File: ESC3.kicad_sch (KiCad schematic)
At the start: 34 parts, among them J11 SWD3, J12 MOTOR3, Q10 XRS306D, Q8 XRS306D, Q9 XRS306D, U11 STM32G071GBUxN, U12 DRV8300D

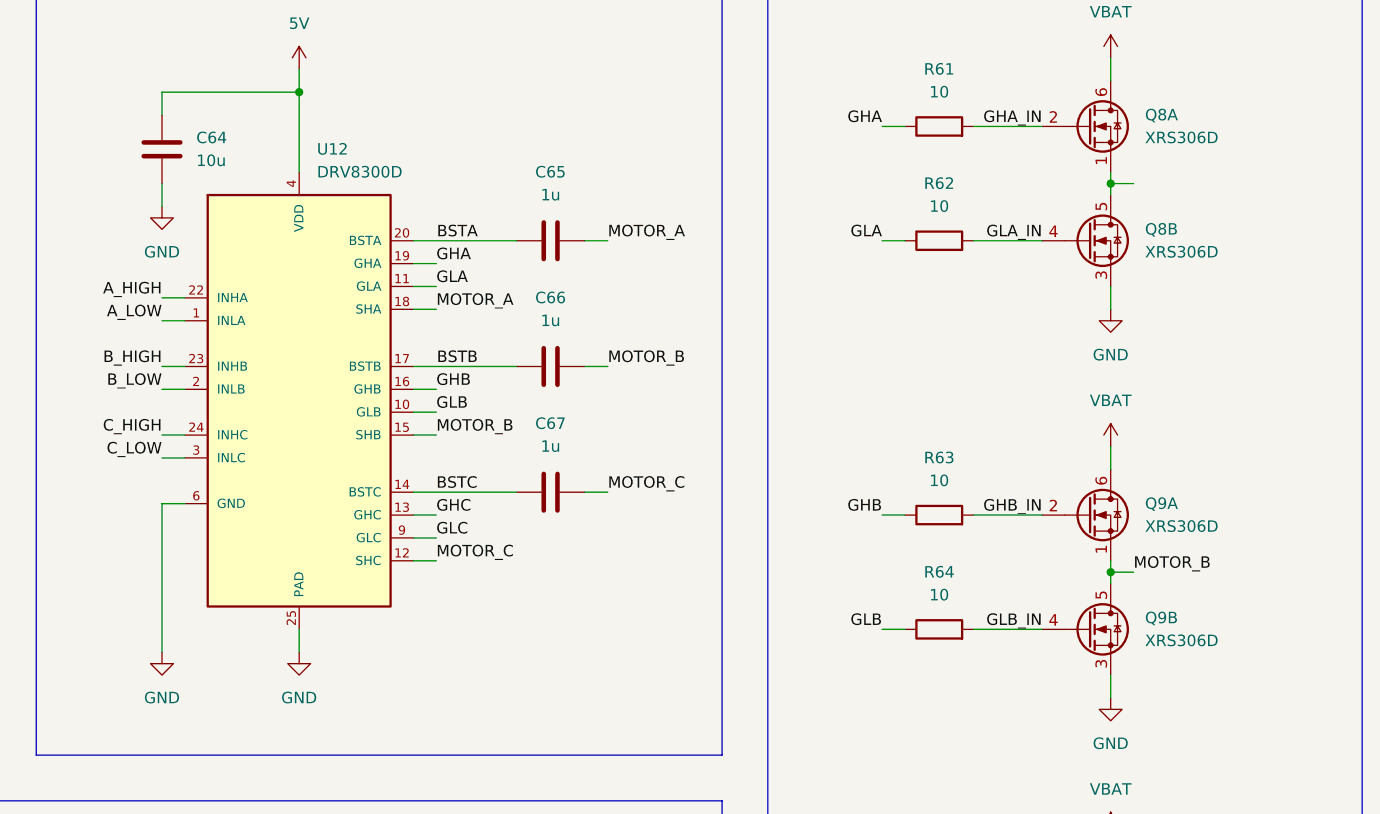
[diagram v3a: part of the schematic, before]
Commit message: Missing labels and revision
First complete revision of the schematic.
Added missing labels.

TODO:
Continue reviewing the schematic.
Include net coloring.
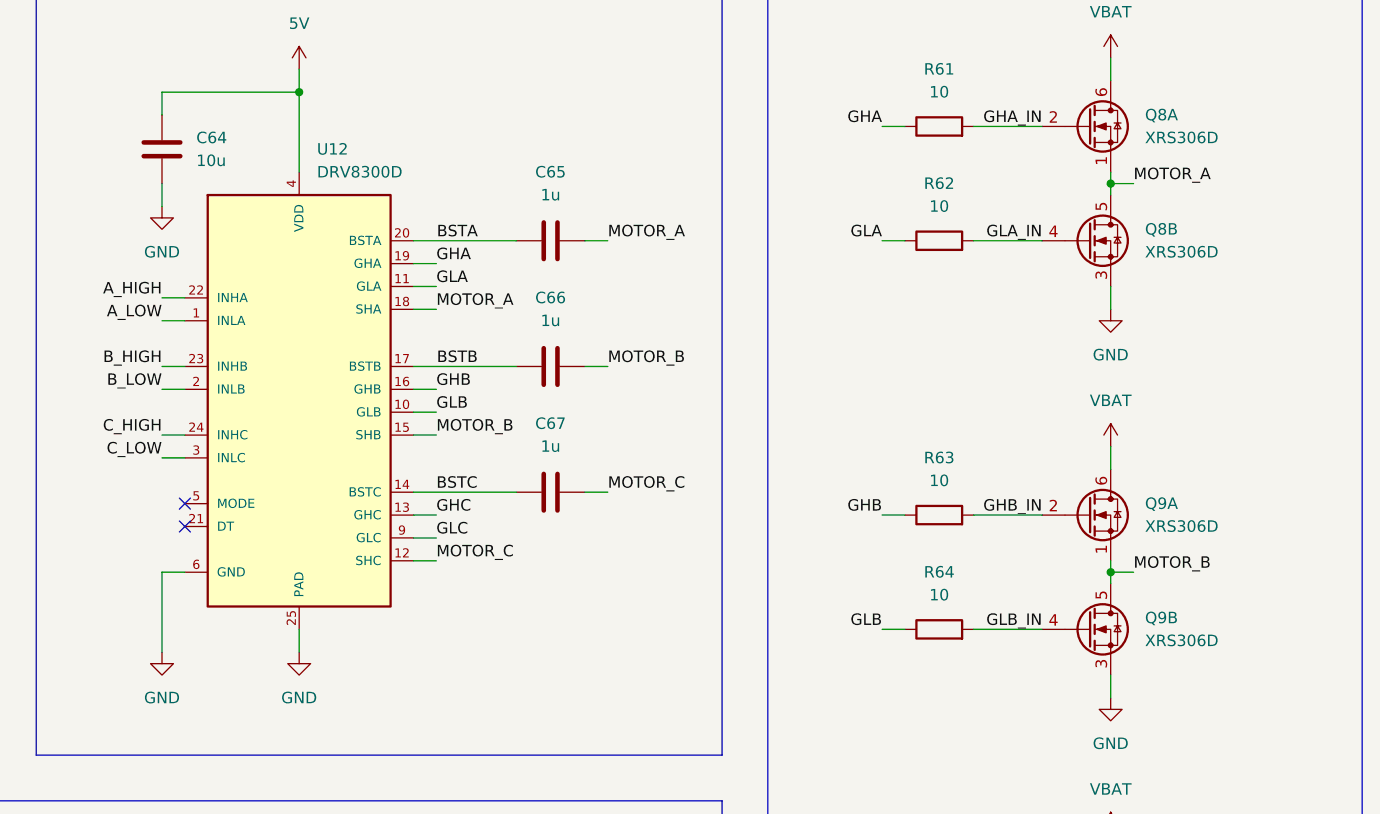
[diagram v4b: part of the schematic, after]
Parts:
- C58, C60, C61, C62, C63: footprint (none) -> Capacitor_SMD:C_1206_3216Metric
- J11: footprint (none) -> Custom_Parts:PAD_2_SQUARE_SOLID_1.0x1.0mm_P1.5mm
- Q10, Q8, Q9: footprint Custom_Parts:PDFN8 -> Custom_Parts:PDFN8_DUAL_3.3x3.3mm
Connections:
- net MOTOR_A: now also Q8.1 (S), Q8.5 (D)
- no-connect marks 13 -> 15
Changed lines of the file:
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@@
 	)
 	(no_connect
+		(at 143.51 81.28)
+	)
+	(no_connect
 		(at 50.8 80.01)
 	)
@@
 	)
 	(no_connect
+		(at 143.51 83.82)
+	)
+	(no_connect
 		(at 50.8 49.53)
 	)
@@
 	(wire
 		(pts
+			(xy 143.51 88.9) (xy 140.97 88.9)
+		)
+		(stroke
+			(width 0)
+			(type default)
+		)
+	)
+	(wire
+		(pts
 			(xy 151.13 133.35) (xy 153.67 133.35)
 		)
@@
 	(wire
 		(pts
-			(xy 143.51 81.28) (xy 140.97 81.28)
+			(xy 140.97 88.9) (xy 140.97 97.79)
 		)
 		(stroke
@@
 	(wire
 		(pts
-			(xy 140.97 81.28) (xy 140.97 97.79)
-		)
-		(stroke
-			(width 0)
-			(type default)
-		)
-	)
-	(wire
-		(pts
 			(xy 62.23 171.45) (xy 62.23 172.72)
 		)
@@
 		)
 	)
+	(label "MOTOR_A"
+		(at 248.92 45.72 0)
+		(effects
+			(font
+				(size 1.27 1.27)
+			)
+			(justify left bottom)
+		)
+	)
 	(label "GHB"
 		(at 220.98 82.55 180)
@@
 			)
 		)
-		(property "Footprint" "Custom_Parts:PDFN8"
+		(property "Footprint" "Custom_Parts:PDFN8_DUAL_3.3x3.3mm"
 			(at 248.92 39.37 0)
 			(effects
@@
 			)
 		)
-		(property "Footprint" ""
+		(property "Footprint" "Capacitor_SMD:C_1206_3216Metric"
 			(at 37.7952 180.34 0)
 			(effects
@@
 			)
 		)
-		(property "Footprint" "Custom_Parts:PDFN8"
+		(property "Footprint" "Custom_Parts:PDFN8_DUAL_3.3x3.3mm"
 			(at 248.92 52.07 0)
 			(effects
@@
 	)
 	(symbol
-		(lib_id "power:GND")
-		(at 140.97 97.79 0)
-		(unit 1)
-		(exclude_from_sim no)
-		(in_bom yes)
-		(on_board yes)
-		(dnp no)
-		(fields_autoplaced yes)
-		(property "Reference" "#PWR0116"
-			(at 140.97 104.14 0)
-			(effects
-				(font
-					(size 1.27 1.27)
-				)
-				(hide yes)
-			)
-		)
-		(property "Value" "GND"
-			(at 140.97 102.87 0)
-			(effects
-				(font
-					(size 1.27 1.27)
-				)
-			)
-		)
-		(property "Footprint" ""
-			(at 140.97 97.79 0)
-			(effects
-				(font
-					(size 1.27 1.27)
-				)
-				(hide yes)
-			)
-		)
-		(property "Datasheet" ""
-			(at 140.97 97.79 0)
-			(effects
-				(font
-					(size 1.27 1.27)
-				)
-				(hide yes)
-			)
-		)
-		(property "Description" "Power symbol creates a global label with name \"GND\" , ground"
-			(at 140.97 97.79 0)
-			(effects
-				(font
-					(size 1.27 1.27)
-				)
-				(hide yes)
-			)
-		)
-		(pin "1"
-		)
-		(instances
-			(project "ThunderHorse"
-				(path "/ac187c6c-fa53-41cc-bce1-6f39a42a92e8/807a5f6f-4255-4cf0-8d90-acd62bb18590/f6401a6f-b04c-410e-81b5-25d3c51023df"
-					(reference "#PWR0116")
-					(unit 1)
-				)
-			)
-		)
-	)
-	(symbol
 		(lib_id "Device:R")
 		(at 144.78 133.35 90)
@@
 			)
 		)
-		(property "Footprint" "Custom_Parts:PDFN8"
+		(property "Footprint" "Custom_Parts:PDFN8_DUAL_3.3x3.3mm"
 			(at 248.92 125.73 0)
 			(effects
@@
 			)
 		)
-		(property "Footprint" "Custom_Parts:PDFN8"
+		(property "Footprint" "Custom_Parts:PDFN8_DUAL_3.3x3.3mm"
 			(at 248.92 82.55 0)
 			(effects
@@
 			)
 		)
-		(property "Footprint" "Custom_Parts:PDFN8"
+		(property "Footprint" "Custom_Parts:PDFN8_DUAL_3.3x3.3mm"
 			(at 248.92 138.43 0)
 			(effects
@@
 		(pin "4"
 		)
+		(pin "7"
+		)
+		(pin "8"
+		)
+		(pin "21"
+		)
+		(pin "5"
+		)
 		(instances
 			(project "ThunderHorse"
@@
 			)
 		)
-		(property "Footprint" ""
+		(property "Footprint" "Capacitor_SMD:C_1206_3216Metric"
 			(at 50.4952 180.34 0)
 			(effects
@@
 			)
 		)
-		(property "Footprint" "Custom_Parts:PDFN8"
+		(property "Footprint" "Custom_Parts:PDFN8_DUAL_3.3x3.3mm"
 			(at 248.92 95.25 0)
 			(effects
@@
 			)
 		)
-		(property "Footprint" ""
+		(property "Footprint" "Capacitor_SMD:C_1206_3216Metric"
 			(at 88.5952 180.34 0)
 			(effects
@@
 			)
 		)
-		(property "Footprint" ""
+		(property "Footprint" "Capacitor_SMD:C_1206_3216Metric"
 			(at 63.1952 180.34 0)
 			(effects
@@
 			)
 		)
-		(property "Footprint" ""
+		(property "Footprint" "Custom_Parts:PAD_2_SQUARE_SOLID_1.0x1.0mm_P1.5mm"
 			(at 102.87 77.47 0)
 			(effects
@@
 			)
 		)
-		(property "Footprint" ""
+		(property "Footprint" "Capacitor_SMD:C_1206_3216Metric"
 			(at 75.8952 180.34 0)
 			(effects
@@
 					(unit 1)
 				)
+			)
+		)
+	)
+	(symbol
+		(lib_id "power:GND")
+		(at 140.97 97.79 0)
+		(unit 1)
+		(exclude_from_sim no)
+		(in_bom yes)
+		(on_board yes)
+		(dnp no)
+		(fields_autoplaced yes)
+		(property "Reference" "#PWR0116"
+			(at 140.97 104.14 0)
+			(effects
+				(font
+					(size 1.27 1.27)
+				)
+				(hide yes)
+			)
+		)
+		(property "Value" "GND"
+			(at 140.97 102.87 0)
+			(effects
+				(font
+					(size 1.27 1.27)
+				)
+			)
+		)
+		(property "Footprint" ""
+			(at 140.97 97.79 0)
+			(effects
+				(font
+					(size 1.27 1.27)
+				)
+				(hide yes)
+			)
+		)
+		(property "Datasheet" ""
+			(at 140.97 97.79 0)
+			(effects
+				(font
+					(size 1.27 1.27)
+				)
+				(hide yes)
+			)
+		)
+		(property "Description" "Power symbol creates a global label with name \"GND\" , ground"
+			(at 140.97 97.79 0)
+			(effects
+				(font
+					(size 1.27 1.27)
+				)
+				(hide yes)
+			)
+		)
+		(pin "1"
+		)
+		(instances
+			(project "ThunderHorse"
+				(path "/ac187c6c-fa53-41cc-bce1-6f39a42a92e8/807a5f6f-4255-4cf0-8d90-acd62bb18590/f6401a6f-b04c-410e-81b5-25d3c51023df"
+					(reference "#PWR0116")
+					(unit 1)
+				)

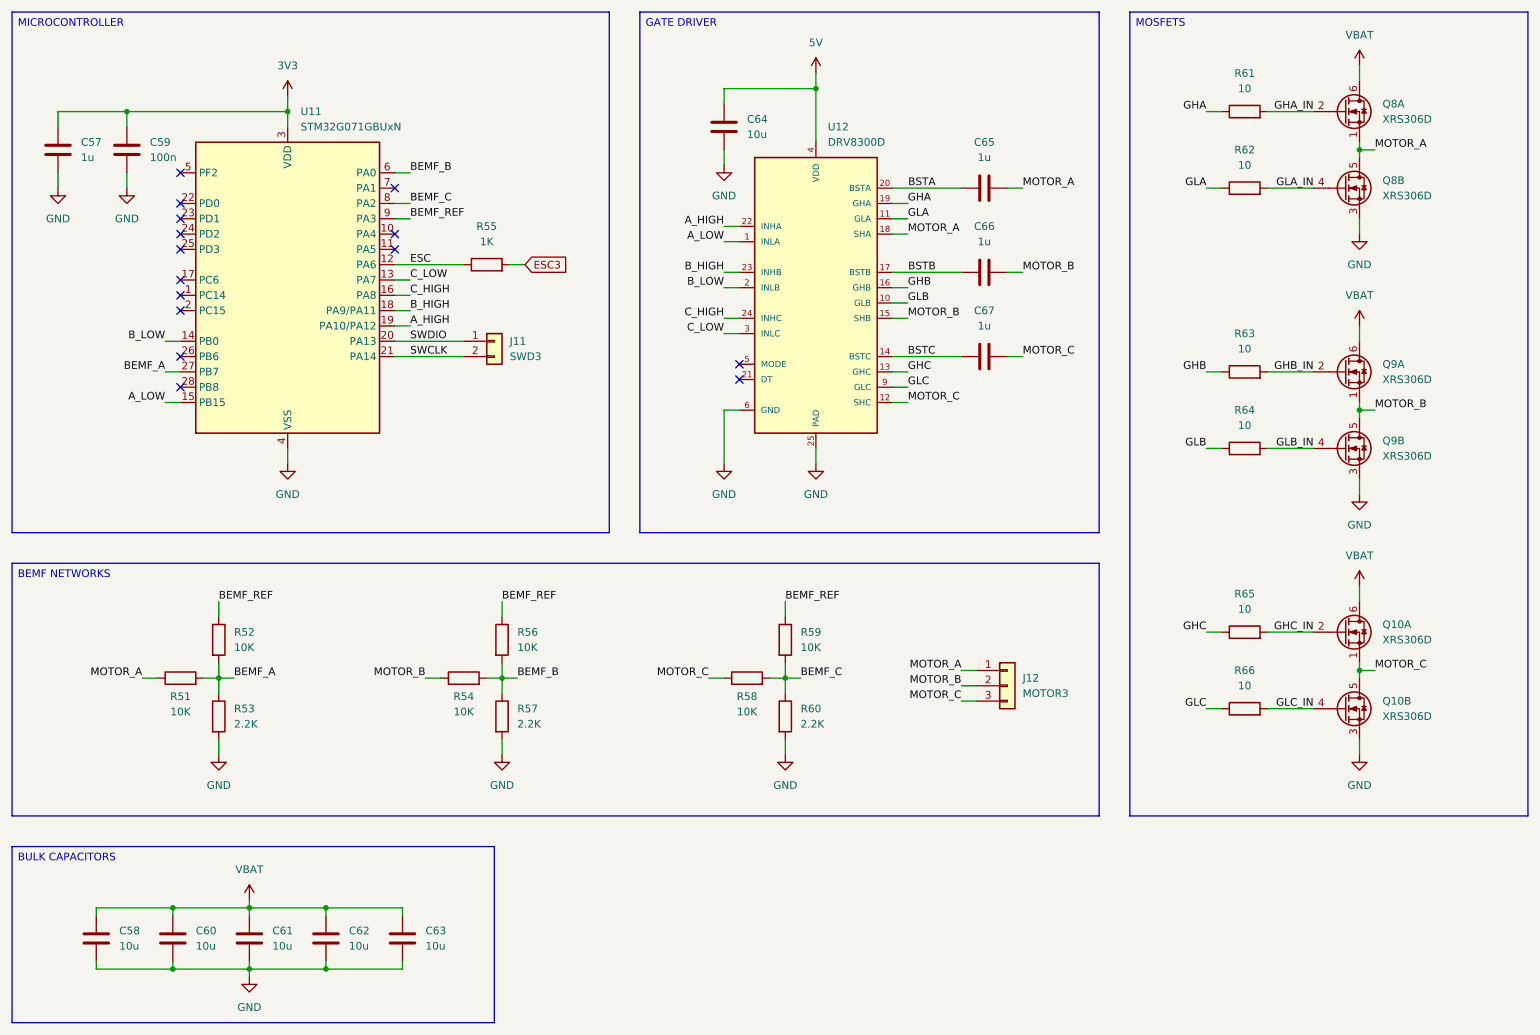
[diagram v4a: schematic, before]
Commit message: ESC layout and footprints
Added the initial ESC layout.
Updated some footprints for compatibility.
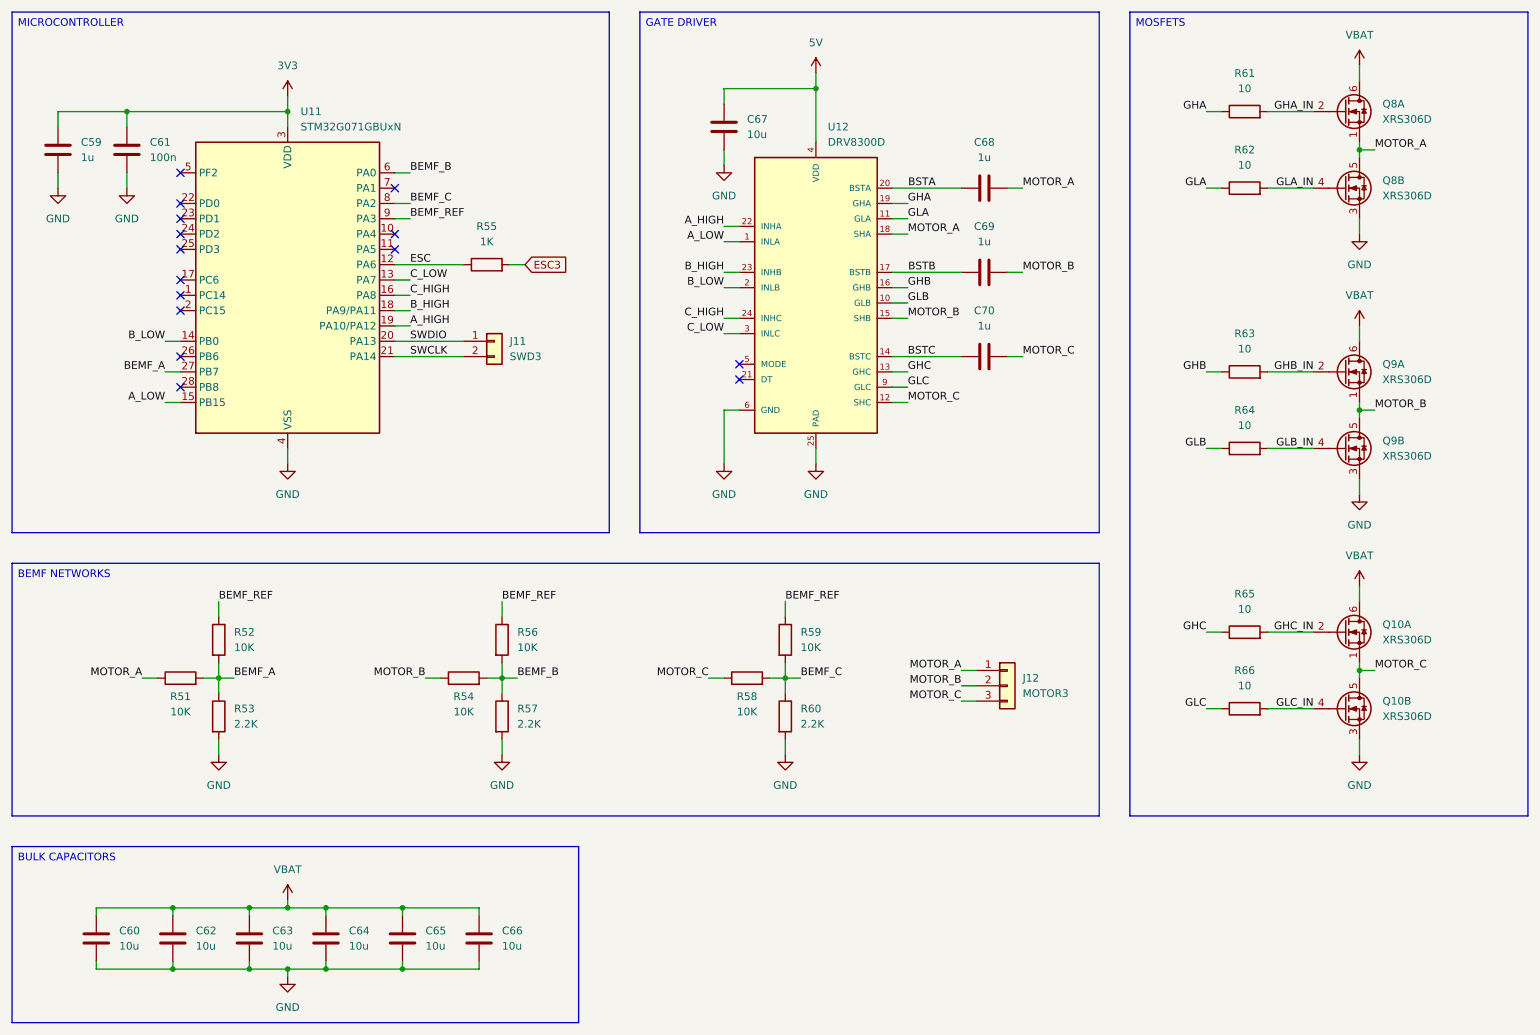
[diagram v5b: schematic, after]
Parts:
- removed C58, C61: 10u, Capacitor_SMD:C_1206_3216Metric, symbol Device:C
- added C64, C65, C66: 10u, Capacitor_SMD:C_1206_3216Metric, symbol Device:C
- J12: footprint Custom_Parts:PAD_3_SQUARE_SOLID_2.0x2.0mm_P2.5mm -> Custom_Parts:PAD_3_SQUARE_SOLID_2.5x2.5mm_P4.0mm
- renumbered C57 to C59, C59 to C61, C64 to C67, C65 to C68, C66 to C69, C67 to C70
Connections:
- net GND: now also C64.2, C65.2, C66.2
- net VBAT: now also C64.1, C65.1, C66.1

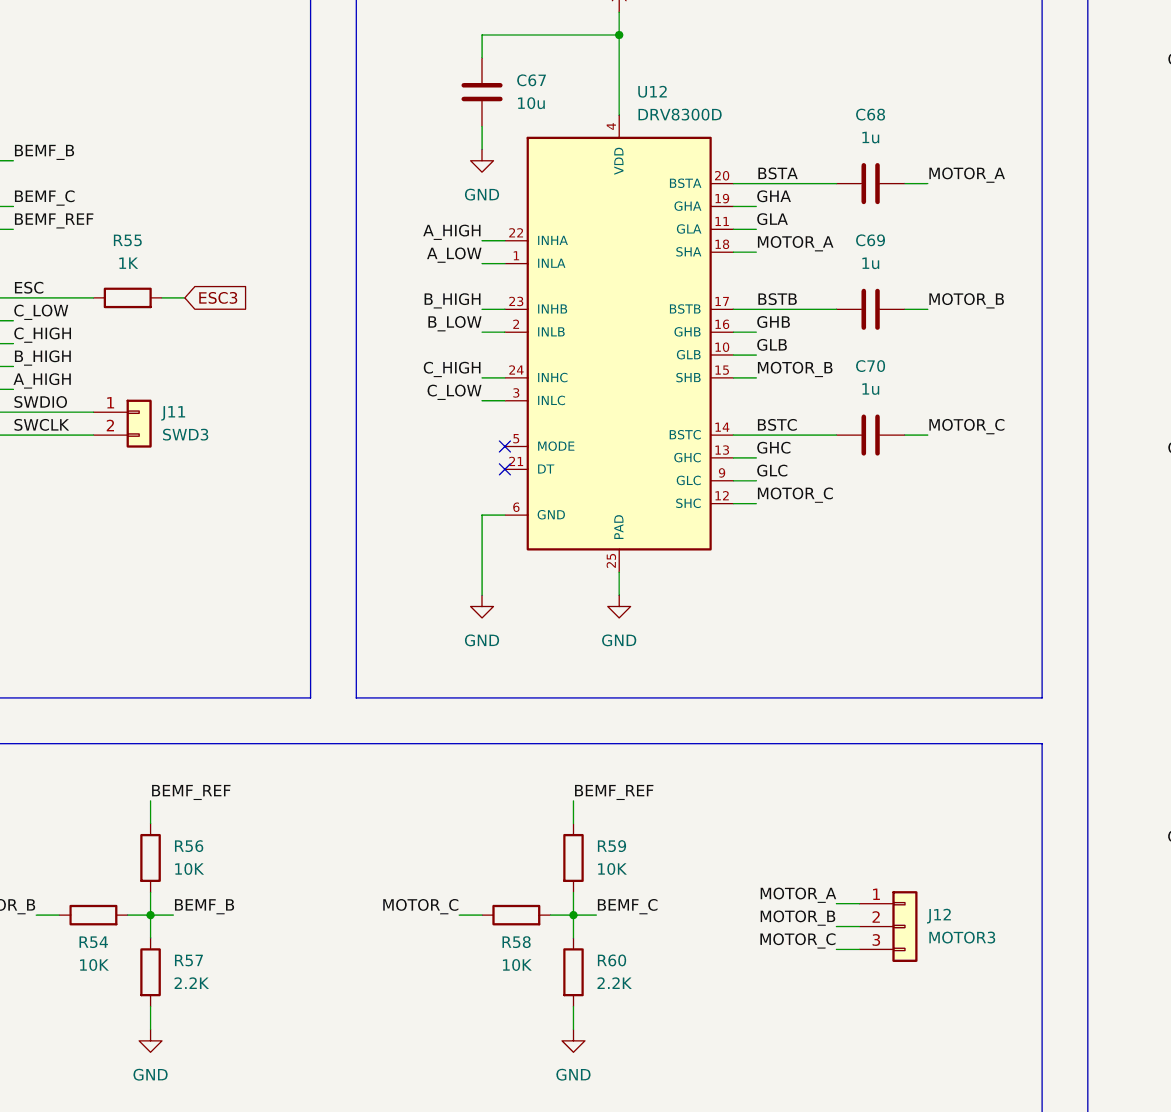
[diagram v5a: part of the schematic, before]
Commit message: Layout replication
Updated the ESC schematic to allow for layout replication.
Updated the PCB layout.
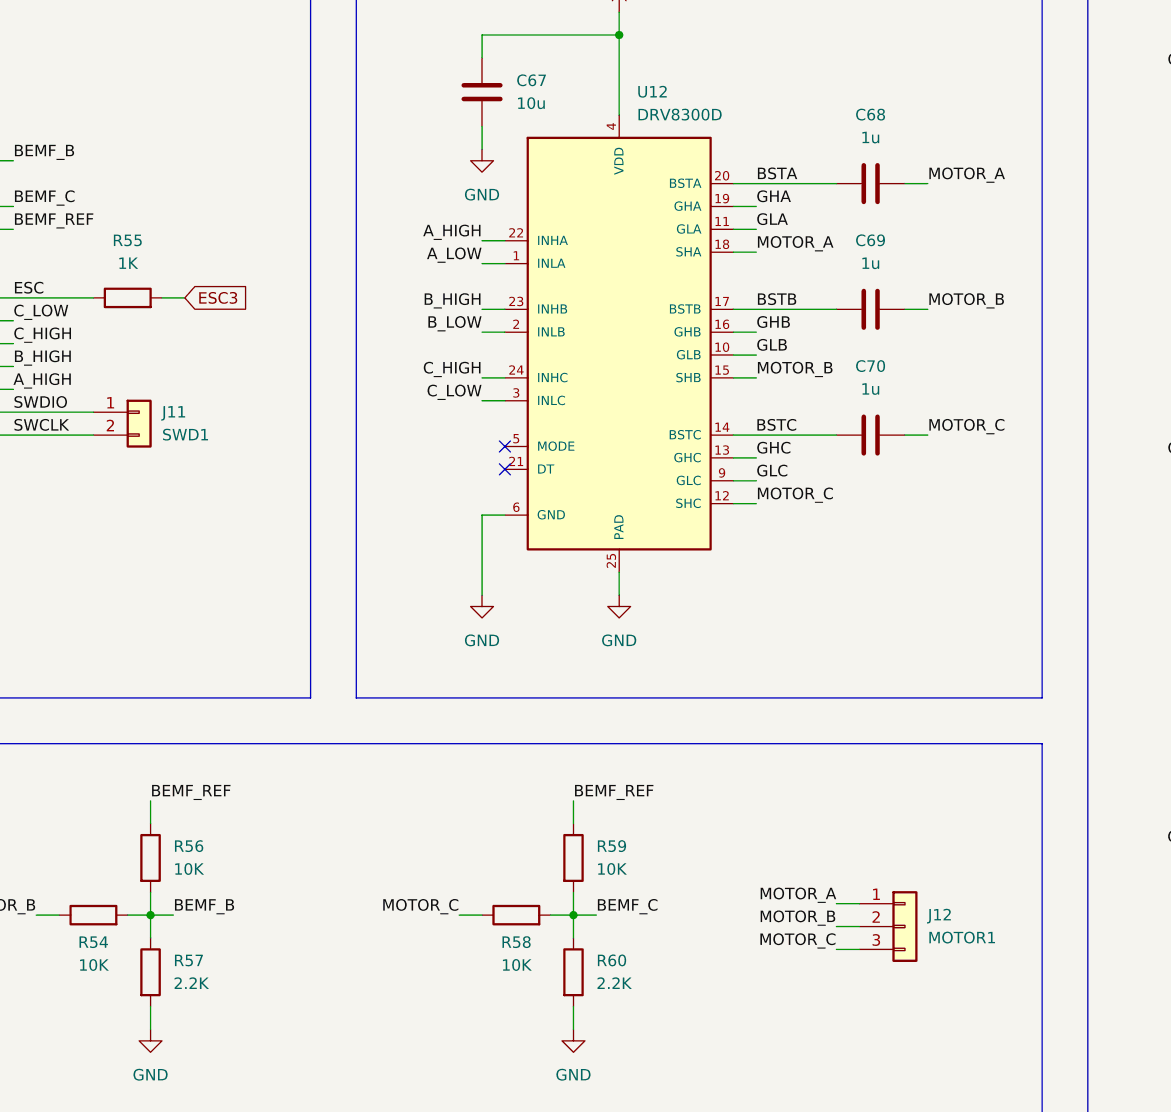
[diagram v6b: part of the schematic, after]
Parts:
- J11: value SWD3 -> SWD1
- J12: value MOTOR3 -> MOTOR1
